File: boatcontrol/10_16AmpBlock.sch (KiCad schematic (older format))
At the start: 13 parts, among them U6101 ULN2803A

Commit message: Switch resistors
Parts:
- removed C6101, C6102, C6103, C6104, C6105, C6106, C6107, C6108: 107CKS016M 100UF, Capacitor_THT:CP_Radial_D5.0mm_P2.00mm, symbol Device:C_Small
- removed RN6101, RN6104: 4116R-1-103LF, DIP787W49P254L2197H469Q16N, symbol BoatControl:4116R-1-103LF
- removed RN6103: 4120R-1-103LF, BoatControl:DIP254P762X432-16P, symbol Device:R_Pack08
- added C7001, C7002, C7003, C7004, C7005, C7006, C7007, C7008: 1uF, Capacitor_THT:C_Disc_D7.5mm_W5.0mm_P5.00mm, symbol Device:C_Small
- added RN?: 10M Ohm, Resistor_THT:R_Array_SIP9, symbol Device:R_Network08
- added RN? (x2): 100K Ohm, Resistor_THT:R_Array_SIP9, symbol Device:R_Network08
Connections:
- wire segments 226 -> 206

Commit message: Resistance is futile
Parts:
- gave numbers to parts that had none: 3
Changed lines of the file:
@@
 $Descr A4 11693 8268
 encoding utf-8
-Sheet 61 87
+Sheet 70 87
 Title "Boat Control Hat"
 Date "2020-07-09"
@@
 AR Path="/D1BB8DB4/5F76AF55/604747A2" Ref="#PWR06101"  Part="1"
 AR Path="/D1BB8DB4/5F75E923/604747A2" Ref="#PWR07001"  Part="1"
-F 0 "#PWR06101" H 6900 3250 50  0001 C CNN
+F 0 "#PWR07001" H 6900 3250 50  0001 C CNN
 F 1 "+12P" H 6750 3500 50  0000 C CNN
 F 2 "" H 6900 3400 50  0001 C CNN
@@
 AR Path="/D1BB8DB4/5F76AF55/604747AF" Ref="U6101"  Part="1"
 AR Path="/D1BB8DB4/5F75E923/604747AF" Ref="U7001"  Part="1"
-F 0 "U6101" H 6450 3500 50  0000 L CNN
+F 0 "U7001" H 6450 3500 50  0000 L CNN
 F 1 "ULN2803A" H 6300 4200 50  0000 L CNN
 F 2 "Package_DIP:DIP-18_W7.62mm" H 6550 3050 50  0001 L CNN
@@
 AR Path="/D1BB8DB4/5F76AF55/604747C1" Ref="#PWR06102"  Part="1"
 AR Path="/D1BB8DB4/5F75E923/604747C1" Ref="#PWR07002"  Part="1"
-F 0 "#PWR06102" H 6500 4150 50  0001 C CNN
+F 0 "#PWR07002" H 6500 4150 50  0001 C CNN
 F 1 "GND" H 6505 4227 50  0000 C CNN
 F 2 "" H 6500 4400 50  0001 C CNN
@@
 AR Path="/D1BB8DB4/5F76AF55/6047484A" Ref="#PWR06103"  Part="1"
 AR Path="/D1BB8DB4/5F75E923/6047484A" Ref="#PWR07003"  Part="1"
-F 0 "#PWR06103" H 2450 5000 50  0001 C CNN
+F 0 "#PWR07003" H 2450 5000 50  0001 C CNN
 F 1 "+5V" H 2465 5323 50  0000 C CNN
 F 2 "" H 2450 5150 50  0001 C CNN
@@
 AR Path="/D1BB8DB4/5F76AF55/60474926" Ref="RN6102"  Part="1"
 AR Path="/D1BB8DB4/5F75E923/60474926" Ref="RN7002"  Part="1"
-F 0 "RN6102" V 7200 3900 50  0000 L CNN
+F 0 "RN7002" V 7200 3900 50  0000 L CNN
 F 1 "4116R-1-471" V 7200 3750 50  0001 L CNN
 F 2 "BoatControl:DIP254P762X432-16P" V 8175 3900 50  0001 C CNN
@@
 AR Path="/D1BB8DB4/5F75E923/62B5C7B5" Ref="C7001"  Part="1"
 AR Path="/D1BB8DB4/5F76AF55/62B5C7B5" Ref="C6101"  Part="1"
-F 0 "C6101" V 4600 2550 50  0000 L CNN
+F 0 "C7001" V 4600 2550 50  0000 L CNN
 F 1 "1uF" H 3800 2400 50  0001 L CNN
 F 2 "Capacitor_THT:C_Disc_D7.5mm_W5.0mm_P5.00mm" H 4650 2500 50  0001 C CNN
@@
 AR Path="/D1BB8DB4/5F75E923/62B76848" Ref="C7002"  Part="1"
 AR Path="/D1BB8DB4/5F76AF55/62B76848" Ref="C6102"  Part="1"
-F 0 "C6102" V 4600 2750 50  0000 L CNN
+F 0 "C7002" V 4600 2750 50  0000 L CNN
 F 1 "1uF" H 3800 2600 50  0001 L CNN
 F 2 "Capacitor_THT:C_Disc_D7.5mm_W5.0mm_P5.00mm" H 4650 2700 50  0001 C CNN
@@
 AR Path="/D1BB8DB4/5F75E923/62B86A50" Ref="C7003"  Part="1"
 AR Path="/D1BB8DB4/5F76AF55/62B86A50" Ref="C6103"  Part="1"
-F 0 "C6103" V 4600 3550 50  0000 L CNN
+F 0 "C7003" V 4600 3550 50  0000 L CNN
 F 1 "1uF" H 3800 3400 50  0001 L CNN
 F 2 "Capacitor_THT:C_Disc_D7.5mm_W5.0mm_P5.00mm" H 4650 3500 50  0001 C CNN
@@
 AR Path="/D1BB8DB4/5F75E923/62B939DB" Ref="C7004"  Part="1"
 AR Path="/D1BB8DB4/5F76AF55/62B939DB" Ref="C6104"  Part="1"
-F 0 "C6104" V 4600 3750 50  0000 L CNN
+F 0 "C7004" V 4600 3750 50  0000 L CNN
 F 1 "1uF" H 3800 3600 50  0001 L CNN
 F 2 "Capacitor_THT:C_Disc_D7.5mm_W5.0mm_P5.00mm" H 4650 3700 50  0001 C CNN
@@
 AR Path="/D1BB8DB4/5F75E923/62BA14CE" Ref="C7005"  Part="1"
 AR Path="/D1BB8DB4/5F76AF55/62BA14CE" Ref="C6105"  Part="1"
-F 0 "C6105" V 4600 4550 50  0000 L CNN
+F 0 "C7005" V 4600 4550 50  0000 L CNN
 F 1 "1uF" H 3800 4400 50  0001 L CNN
 F 2 "Capacitor_THT:C_Disc_D7.5mm_W5.0mm_P5.00mm" H 4650 4500 50  0001 C CNN
@@
 AR Path="/D1BB8DB4/5F75E923/62BAE342" Ref="C7006"  Part="1"
 AR Path="/D1BB8DB4/5F76AF55/62BAE342" Ref="C6106"  Part="1"
-F 0 "C6106" V 4600 4750 50  0000 L CNN
+F 0 "C7006" V 4600 4750 50  0000 L CNN
 F 1 "1uF" H 3800 4600 50  0001 L CNN
 F 2 "Capacitor_THT:C_Disc_D7.5mm_W5.0mm_P5.00mm" H 4650 4700 50  0001 C CNN
@@
 AR Path="/D1BB8DB4/5F75E923/62BBBC28" Ref="C7007"  Part="1"
 AR Path="/D1BB8DB4/5F76AF55/62BBBC28" Ref="C6107"  Part="1"
-F 0 "C6107" V 4600 5550 50  0000 L CNN
+F 0 "C7007" V 4600 5550 50  0000 L CNN
 F 1 "1uF" H 3800 5400 50  0001 L CNN
 F 2 "Capacitor_THT:C_Disc_D7.5mm_W5.0mm_P5.00mm" H 4650 5500 50  0001 C CNN
@@
 AR Path="/D1BB8DB4/5F75E923/62BC8A92" Ref="C7008"  Part="1"
 AR Path="/D1BB8DB4/5F76AF55/62BC8A92" Ref="C6108"  Part="1"
-F 0 "C6108" V 4600 5750 50  0000 L CNN
+F 0 "C7008" V 4600 5750 50  0000 L CNN
 F 1 "1uF" H 3800 5600 50  0001 L CNN
 F 2 "Capacitor_THT:C_Disc_D7.5mm_W5.0mm_P5.00mm" H 4650 5700 50  0001 C CNN
@@
 AR Path="/D16552B4/5FA17F6C/62CB5764" Ref="RN?"  Part="1"
 AR Path="/D1BB8DB4/5F317CB5/62CB5764" Ref="RN?"  Part="1"
-AR Path="/D1BB8DB4/5F75E923/62CB5764" Ref="RN?"  Part="1"
-AR Path="/D1BB8DB4/5F76AF55/62CB5764" Ref="RN?"  Part="1"
-F 0 "RN?" V 2150 3900 50  0000 L CNN
+AR Path="/D1BB8DB4/5F75E923/62CB5764" Ref="RN7003"  Part="1"
+AR Path="/D1BB8DB4/5F76AF55/62CB5764" Ref="RN6103"  Part="1"
+F 0 "RN7003" V 2150 3900 50  0000 L CNN
 F 1 "10M Ohm" H 2300 3550 50  0001 L CNN
 F 2 "Resistor_THT:R_Array_SIP9" V 3125 3950 50  0001 C CNN
@@
 AR Path="/D16552B4/5FA17F6C/630078FE" Ref="RN?"  Part="1"
 AR Path="/D16552B4/5FA17F86/630078FE" Ref="RN?"  Part="1"
-F 0 "RN?" V 2150 3050 50  0000 C CNN
+AR Path="/D1BB8DB4/5F76AF55/630078FE" Ref="RN6101"  Part="1"
+AR Path="/D1BB8DB4/5F75E923/630078FE" Ref="RN7001"  Part="1"
+F 0 "RN7001" V 2150 3050 50  0000 C CNN
 F 1 "100K Ohm" V 2450 2750 50  0001 C CNN
 F 2 "Resistor_THT:R_Array_SIP9" H 3400 3150 50  0001 L CNN
@@
 AR Path="/D16552B4/5FA17F6C/63015012" Ref="RN?"  Part="1"
 AR Path="/D16552B4/5FA17F86/63015012" Ref="RN?"  Part="1"
-F 0 "RN?" V 2150 4850 50  0000 C CNN
+AR Path="/D1BB8DB4/5F76AF55/63015012" Ref="RN6104"  Part="1"
+AR Path="/D1BB8DB4/5F75E923/63015012" Ref="RN7004"  Part="1"
+F 0 "RN7004" V 2150 4850 50  0000 C CNN
 F 1 "100K Ohm" V 2450 4550 50  0001 C CNN
 F 2 "Resistor_THT:R_Array_SIP9" H 3400 4950 50  0001 L CNN

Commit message: Add reverse/AC/DC polarity indicators
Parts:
- RN6102: value 4116R-1-471 -> 680Ohm; Field4 470 Ohm -> 4116R-1-681LF‎
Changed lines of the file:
@@
 AR Path="/D1BB8DB4/5F75E923/60474926" Ref="RN7002"  Part="1"
 F 0 "RN7002" V 7200 3900 50  0000 L CNN
-F 1 "4116R-1-471" V 7200 3750 50  0001 L CNN
+F 1 "680Ohm" V 7200 3750 50  0001 L CNN
 F 2 "BoatControl:DIP254P762X432-16P" V 8175 3900 50  0001 C CNN
 F 3 "https://www.bourns.com/docs/Product-Datasheets/4100R.pdf" H 7700 3900 50  0001 C CNN
-F 4 "470 Ohm" V 7700 3900 50  0001 C CNN "Field4"
+F 4 "4116R-1-681LF‎" V 7700 3900 50  0001 C CNN "Field4"
 	1    7700 3900
 	0    1    1    0

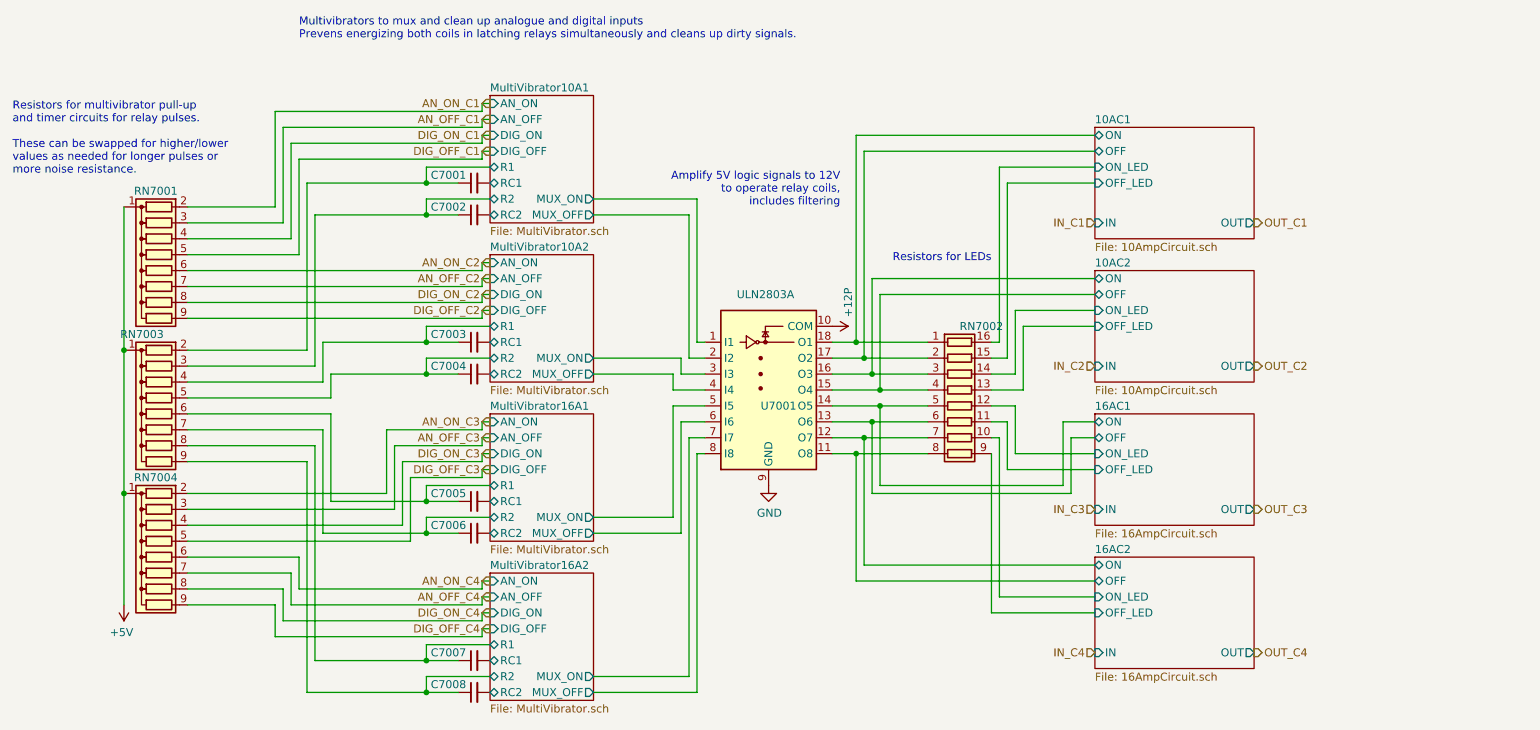
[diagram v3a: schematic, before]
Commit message: Fix LED resistors
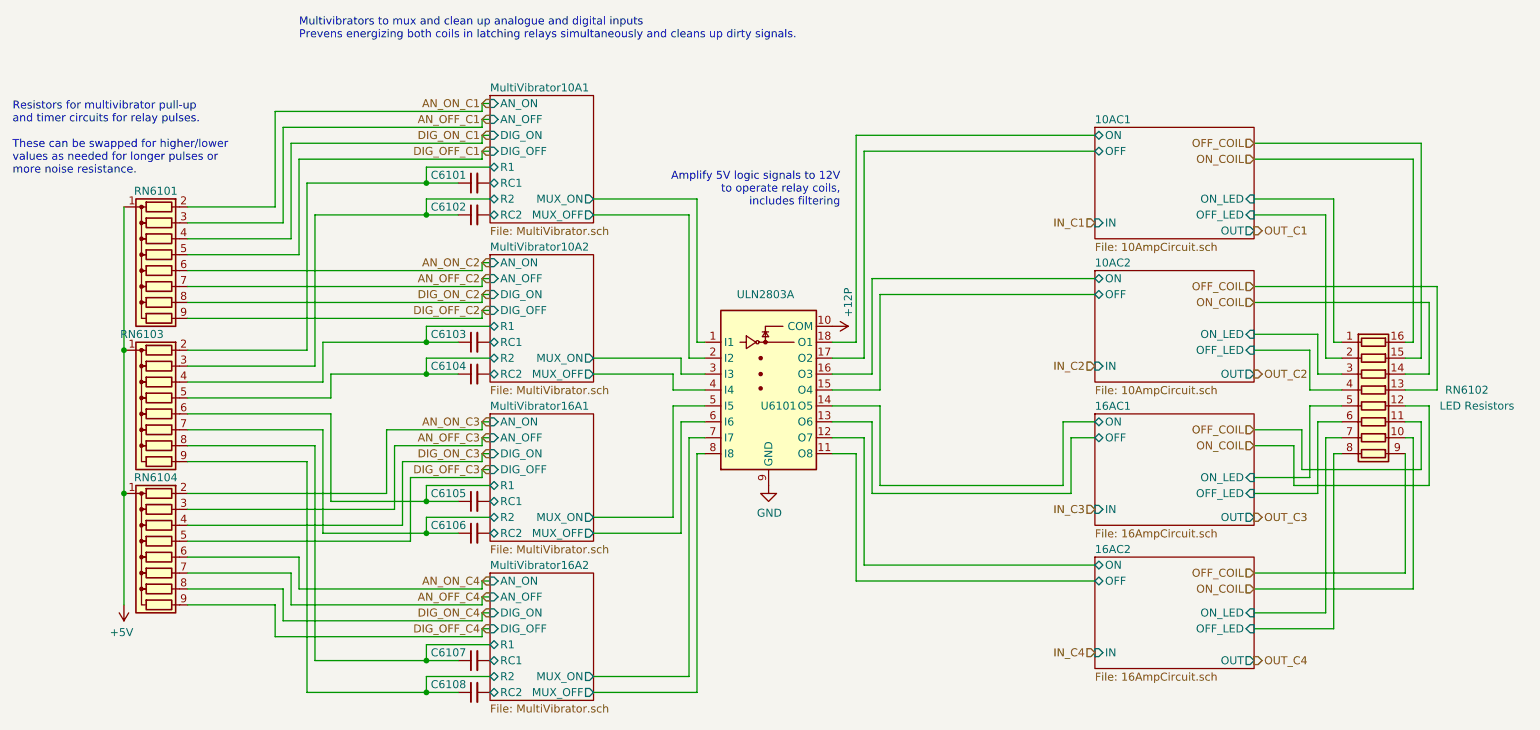
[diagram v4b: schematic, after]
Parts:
- RN6102: Purpose (none) -> LED Resistors
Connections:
- net 10AC1/OFF: no longer RN6102.2 (R2.1)
- net 10AC1/OFF_LED: now also RN6102.2 (R2.1); no longer RN6102.15 (R2.2)
- net 10AC1/ON: no longer RN6102.1 (R1.1)
- net 10AC1/ON_LED: now also RN6102.1 (R1.1); no longer RN6102.16 (R1.2)
- net 10AC2/OFF: no longer RN6102.4 (R4.1)
- net 10AC2/OFF_LED: now also RN6102.4 (R4.1); no longer RN6102.13 (R4.2)
- net 10AC2/ON: no longer RN6102.3 (R3.1)
- net 10AC2/ON_LED: now also RN6102.3 (R3.1); no longer RN6102.14 (R3.2)
- net 16AC1/OFF: no longer RN6102.6 (R6.1)
- net 16AC1/OFF_LED: now also RN6102.6 (R6.1); no longer RN6102.11 (R6.2)
- net 16AC1/ON: no longer RN6102.5 (R5.1)
- net 16AC1/ON_LED: now also RN6102.5 (R5.1); no longer RN6102.12 (R5.2)
- net 16AC2/OFF: no longer RN6102.8 (R8.1)
- net 16AC2/OFF_LED: now also RN6102.8 (R8.1); no longer RN6102.9 (R8.2)
- net 16AC2/ON: no longer RN6102.7 (R7.1)
- net 16AC2/ON_LED: now also RN6102.7 (R7.1); no longer RN6102.10 (R7.2)
- new net OFF_COIL: RN6102.11 (R6.2), RN6102.13 (R4.2), RN6102.15 (R2.2), RN6102.9 (R8.2)
- new net ON_COIL: RN6102.10 (R7.2), RN6102.12 (R5.2), RN6102.14 (R3.2), RN6102.16 (R1.2)
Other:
- note removed: "Resistors for LEDs"
- moved on the sheet: RN6102

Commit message: Before re-order
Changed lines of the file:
@@
 Wire Wire Line
 	7050 5000 8550 5000
-$Sheet
-S 8550 2150 1000 700
-U 60474911
-F0 "10AC1" 50
-F1 "10AmpCircuit.sch" 50
-F2 "ON" B L 8550 2200 50
-F3 "OFF" B L 8550 2300 50
-F4 "ON_LED" I R 9550 2600 50
-F5 "OFF_LED" I R 9550 2700 50
-F6 "OUT" O R 9550 2800 50
-F7 "IN" I L 8550 2750 50
-$EndSheet
-$Sheet
-S 8550 3950 1000 700
-U 604748FF
-F0 "16AC1" 50
-F1 "16AmpCircuit.sch" 50
-F2 "ON" B L 8550 4000 50
-F3 "OFF" B L 8550 4100 50
-F4 "ON_LED" I R 9550 4350 50
-F5 "OFF_LED" I R 9550 4450 50
-F6 "OUT" O R 9550 4600 50
-F7 "IN" I L 8550 4550 50
-$EndSheet
 $Comp
 L Device:C_Small C?
@@
 	9950 3700 10100 3700
 Wire Wire Line
-	9550 2700 10000 2700
-Wire Wire Line
-	10000 2700 10000 3600
-Wire Wire Line
 	10000 3600 10100 3600
 Wire Wire Line
-	9550 2600 10050 2600
-Wire Wire Line
 	10050 3500 10100 3500
-Wire Wire Line
-	10050 2600 10050 3500
 Wire Wire Line
 	10500 3600 10600 3600
@@
 Text HLabel 9550 5050 0    50   Input ~ 0
 ON_COIL
+$Sheet
+S 8550 3950 1000 700
+U 604748FF
+F0 "16AC1" 50
+F1 "16AmpCircuit.sch" 50
+F2 "ON" B L 8550 4000 50
+F3 "OFF" B L 8550 4100 50
+F4 "ON_LED" I R 9550 4350 50
+F5 "OFF_LED" I R 9550 4450 50
+F6 "OUT" O R 9550 4600 50
+F7 "IN" I L 8550 4550 50
+$EndSheet
+$Sheet
+S 8550 2150 1000 700
+U 60474911
+F0 "10AC1" 50
+F1 "10AmpCircuit.sch" 50
+F2 "ON" B L 8550 2200 50
+F3 "OFF" B L 8550 2300 50
+F4 "ON_LED" I R 9550 2550 50
+F5 "OFF_LED" I R 9550 2650 50
+F6 "OUT" O R 9550 2800 50
+F7 "IN" I L 8550 2750 50
+$EndSheet
+Wire Wire Line
+	10050 2550 9550 2550
+Wire Wire Line
+	10050 2550 10050 3500
+Wire Wire Line
+	9550 2650 10000 2650
+Wire Wire Line
+	10000 2650 10000 3600
 $EndSCHEMATC
